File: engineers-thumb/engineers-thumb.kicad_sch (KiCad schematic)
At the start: 36 parts, among them J1 Barrel_Jack_Switch, J2 AudioJack3_Switch, Q1 BC556, Q2 J112, U1 ICL7660

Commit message: Intermittent eng thumb redux
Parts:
- added U? (x5): LM13700, symbol Amplifier_Operational:LM13700
- gave numbers to parts that had none: 13
- renumbered U1 to U2

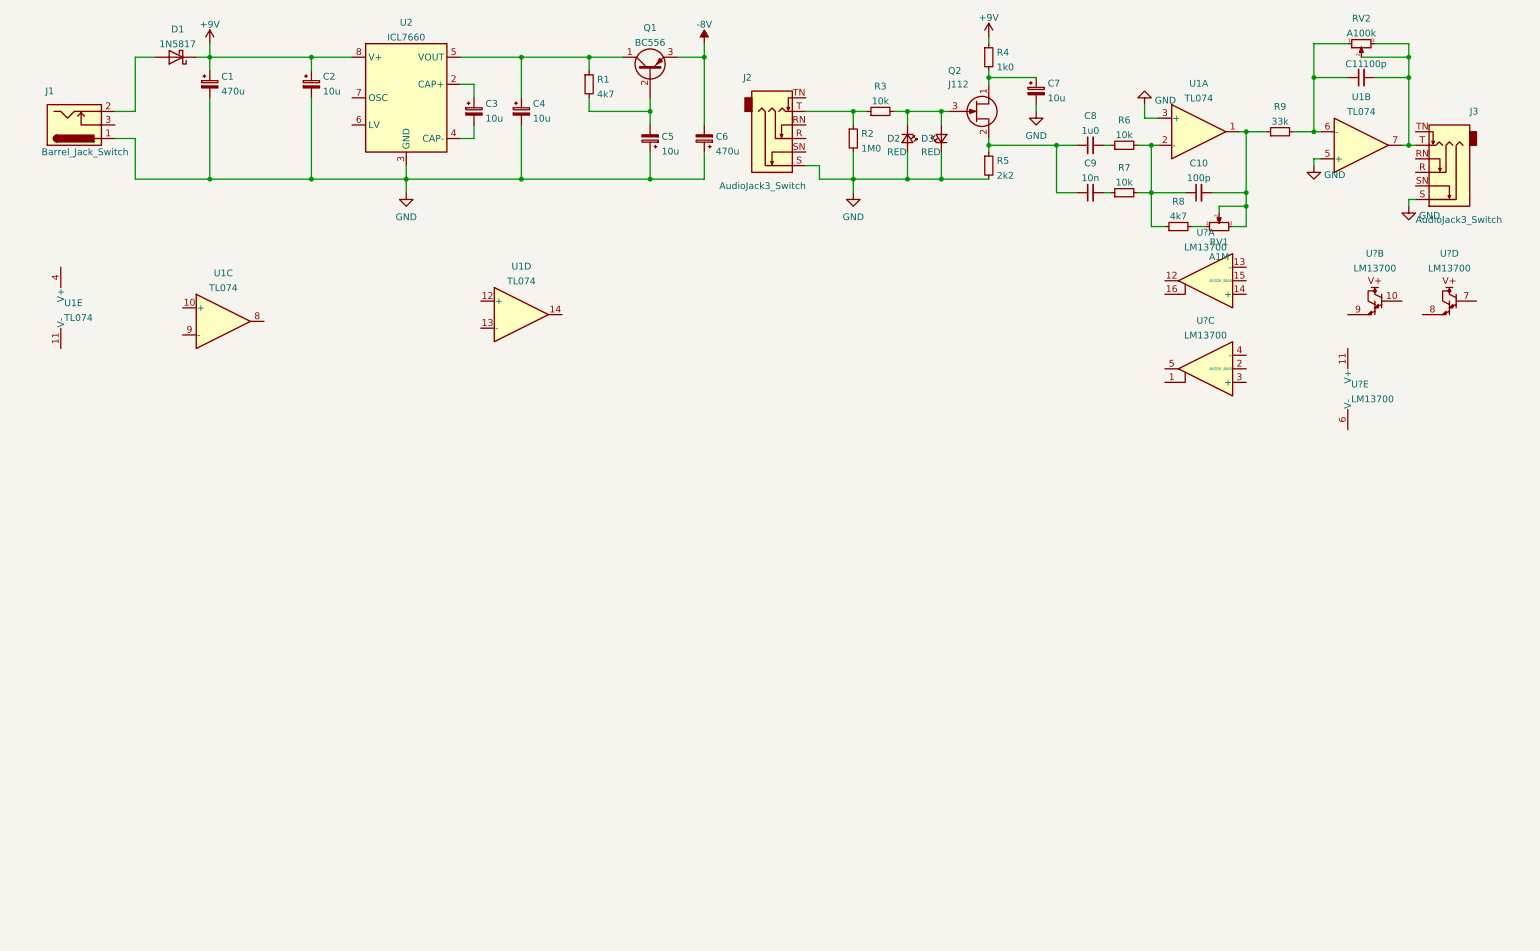
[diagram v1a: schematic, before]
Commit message: Engineers Thumb 1st. cancdidate
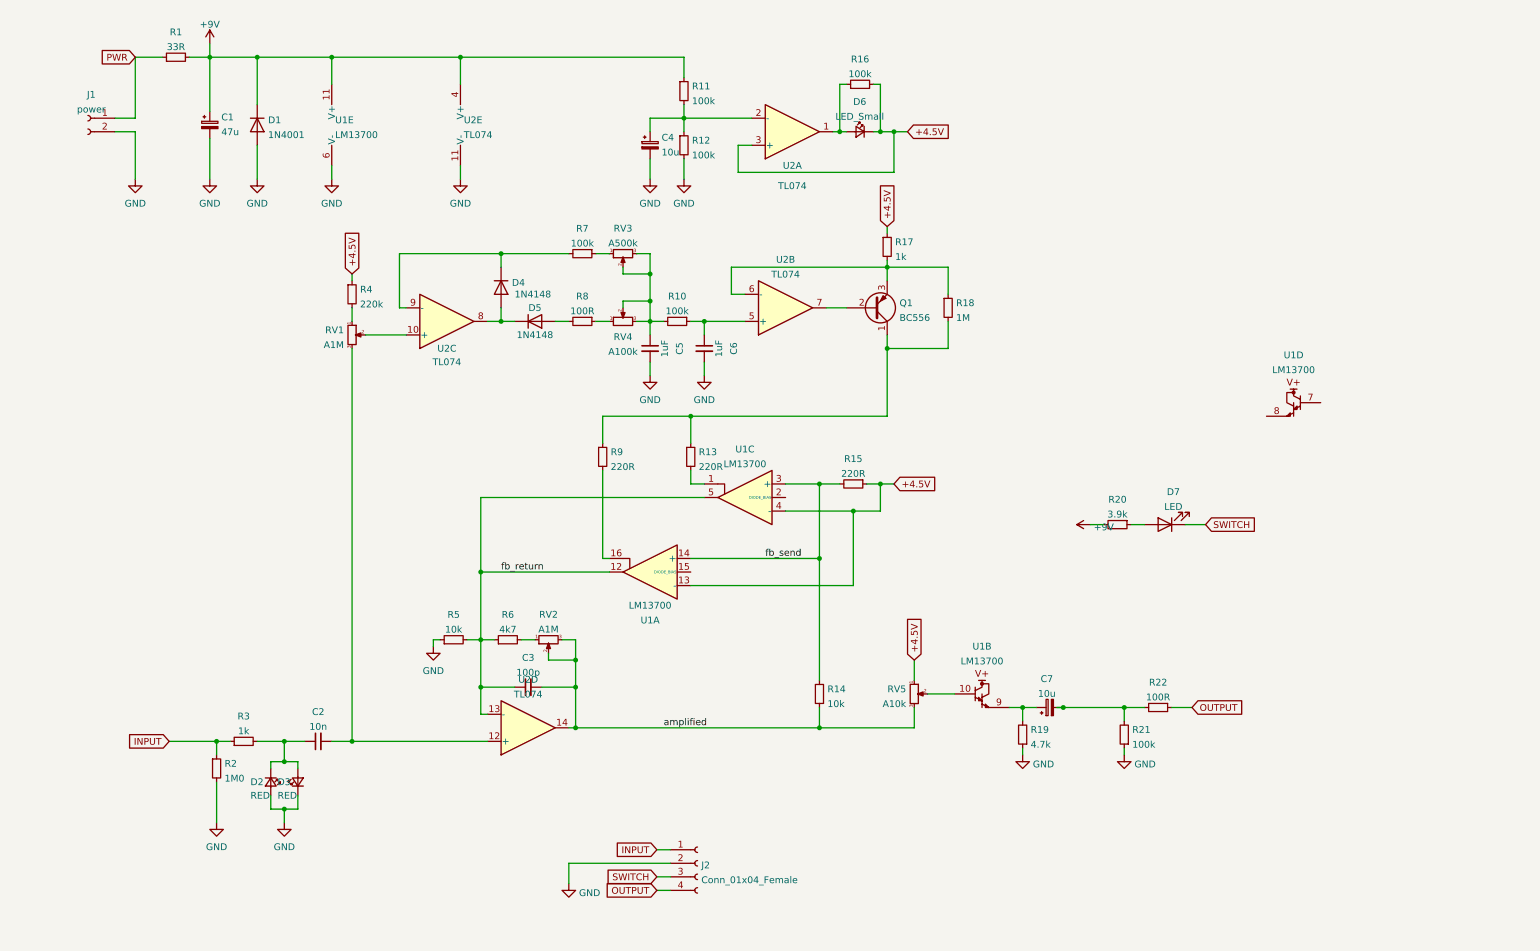
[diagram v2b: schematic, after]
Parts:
- removed C10, C11: 100p, Capacitor_THT:C_Disc_D5.0mm_W2.5mm_P2.50mm, symbol Device:C_Small
- removed C3, C4, C5: 10u, Capacitor_THT:CP_Radial_D5.0mm_P2.50mm, symbol Device:CP_Small
- removed C6: 470u, Capacitor_THT:CP_Radial_D10.0mm_P5.00mm, symbol Device:CP_Small
- removed C8: 1u0, Capacitor_THT:C_Rect_L7.0mm_W4.5mm_P5.00mm, symbol Device:C_Small
- removed D1: 1N5817, Diode_THT:D_DO-41_SOD81_P10.16mm_Horizontal, symbol Diode:1N5817
- removed J1: Barrel_Jack_Switch, Connector_BarrelJack:BarrelJack_Horizontal, symbol Connector:Barrel_Jack_Switch
- removed J2, J3: AudioJack3_Switch, PartsStash:Jack_6.35mm_Rean_NYS215_Horizontal, symbol Connector:AudioJack3_Switch
- removed Q2: J112, Package_TO_SOT_THT:TO-92L_Inline_Wide, symbol Transistor_FET:MMBFJ112
- removed U2: ICL7660, Package_DIP:DIP-8_W7.62mm_LongPads, symbol Regulator_SwitchedCapacitor:ICL7660
- added C3: 100p, Capacitor_THT:C_Disc_D5.0mm_W2.5mm_P2.50mm, symbol Device:C_Small
- added C5, C6: 1uF, Capacitor_THT:C_Rect_L7.0mm_W2.5mm_P5.00mm, symbol Device:C_Small
- added D1: 1N4001, Diode_THT:D_DO-41_SOD81_P10.16mm_Horizontal, symbol Diode:1N4001
- added D4, D5: 1N4148, Diode_THT:D_DO-35_SOD27_P7.62mm_Horizontal, symbol Diode:1N4148
- added D6: LED_Small, LED_THT:LED_D3.0mm_Clear, symbol Device:LED_Small
- added D7: LED, LED_THT:LED_D3.0mm, symbol Device:LED
- added J1: power, Connector_Wire:SolderWire-0.1sqmm_1x02_P3.6mm_D0.4mm_OD1mm, symbol Connector:Conn_01x02_Female
- added J2: Conn_01x04_Female, Connector_Wire:SolderWire-0.1sqmm_1x04_P3.6mm_D0.4mm_OD1mm, symbol Connector:Conn_01x04_Female
- added R10, R11, R12, R16, R21: 100k, PartsStash:R_Axial_DIN0207_L6.3mm_D2.5mm_P7.62mm_Horizontal, symbol Device:R_Small
- added R13, R15, R9: 220R, PartsStash:R_Axial_DIN0207_L6.3mm_D2.5mm_P7.62mm_Horizontal, symbol Device:R_Small
- added R14: 10k, PartsStash:R_Axial_DIN0207_L6.3mm_D2.5mm_P7.62mm_Horizontal, symbol Device:R_Small
- added R17: 1k, PartsStash:R_Axial_DIN0207_L6.3mm_D2.5mm_P7.62mm_Horizontal, symbol Device:R_Small
- added R18: 1M, PartsStash:R_Axial_DIN0207_L6.3mm_D2.5mm_P7.62mm_Horizontal, symbol Device:R_Small
- added R20: 3.9k, PartsStash:R_Axial_DIN0207_L6.3mm_D2.5mm_P7.62mm_Horizontal, symbol Device:R_Small
- added R22: 100R, PartsStash:R_Axial_DIN0207_L6.3mm_D2.5mm_P7.62mm_Horizontal, symbol Device:R_Small
- added RV2: A1M, Connector_PinHeader_2.54mm:PinHeader_1x03_P2.54mm_Vertical, symbol Device:R_POT_Small
- added RV3: A500k, Connector_PinHeader_2.54mm:PinHeader_1x03_P2.54mm_Vertical, symbol Device:R_POT_Small
- added RV4: A100k, Connector_PinHeader_2.54mm:PinHeader_1x03_P2.54mm_Vertical, symbol Device:R_POT_Small
- C1: value 470u -> 47u; footprint Capacitor_THT:CP_Radial_D10.0mm_P5.00mm -> Capacitor_THT:CP_Radial_D8.0mm_P3.50mm
- Q1: footprint Package_TO_SOT_THT:TO-92_Inline -> Package_TO_SOT_THT:TO-92_Inline_Wide
- R1: value 4k7 -> 33R
- R19: renamed from R9; value 33k -> 4.7k
- R3: value 10k -> 1k
- R4: value 1k0 -> 220k
- R5: value 2k2 -> 10k
- R6: value 10k -> 4k7
- R7: value 10k -> 100k
- R8: value 4k7 -> 100R
- RV5: renamed from RV2; value A100k -> A10k; footprint Connector_PinHeader_2.54mm:PinHeader_1x03_P2.54mm_Vertical -> Connector_Wire:SolderWire-0.1sqmm_1x03_P3.6mm_D0.4mm_OD1mm
- U1: renamed from U?; footprint (none) -> Package_DIP:DIP-16_W7.62mm_LongPads
- U2: renamed from U1; footprint (none) -> Package_DIP:DIP-14_W7.62mm_Socket_LongPads
- renumbered C9 to C2, C2 to C4
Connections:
- net +9V: now also R1.2, U1.11 (V+), U2.4 (V+), D1.1 (K), R11.1, R20.2; no longer C4.1, R4.1
- net GND: now also R19.1, R5.1, U1.6 (V-), U2.11 (V-), C5.2, C6.2, D1.2 (A), J1.2 (Pin_2), J2.2 (Pin_2), R12.2, R21.1; no longer C7.2, R5.2, U2.3 (+), U2.5 (+)
- net at C2.1: now also D2.1 (K), D3.2 (A), R3.2; no longer R5.1
- net fb_return: now reaches R6.1
- net fb_return: now also R5.2, U1.12, U1.5, U2.13 (-), C3.1
- net at Q1.2 (B): now also U2.7; no longer R1.2
- net at Q1.1 (C): now also R13.1, R18.2, R9.1; no longer R1.1
- net at R8.2: now also D5.2 (A); no longer RV1.1
- net +4.5V: now reaches U1.13 (-)
- net +4.5V: now also R4.1, RV5.1, U1.4 (-), U2.3 (+), D6.1 (K), R15.1, R16.2, R17.1
- net fb_send: now reaches U1.14 (+)
- net fb_send: now also U1.3 (+), R14.2, R15.2
- net at U1.16: now also R9.2
- net at C7.1: now also R19.2, U1.9; no longer R4.2
- net at U1.10: now also RV5.2
- net at U2.12 (+): now also C2.2, RV1.3
- net amplified: now reaches U2.14
- net amplified: now also RV5.3, C3.2, R14.1, RV2.2, RV2.3
- net at R7.1: now also RV3.1; no longer C2.2
- net INPUT: now reaches R2.1, R3.1
- net INPUT: now also J2.1 (Pin_1)
- net at U1.1: now also R13.2
- net at U2.10 (+): now also RV1.2
- net at U2.8: now also D4.2 (A), D5.1 (K)
- net at U2.9 (-): now also R7.2, D4.1 (K)
- net -8V: no longer names the net of Q1.3 (E)
- net -8V: now also U2.6 (-), R17.2, R18.1
- new net: C6.1, R10.1, U2.5 (+)
- new net: C5.1, R10.2, RV3.2, RV3.3, RV4.2, RV4.3
- new net: R8.1, RV4.1
- new net: C4.1, R11.2, R12.1, U2.2 (-)
- new net: D6.2 (A), R16.1, U2.1
- new net: C7.2, R21.2, R22.2
- new net: R6.2, RV2.1
- new net: D7.2 (A), R20.1
- new net: R4.2, RV1.1
- new net OUTPUT: J2.4 (Pin_4), R22.1
- new net PWR: J1.1 (Pin_1), R1.1
- new net SWITCH: D7.1 (K), J2.3 (Pin_3)
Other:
- moved on the sheet: C1, C2, C4, D2, D3, R19, R2, R3, R4, RV5, U1A, U1B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

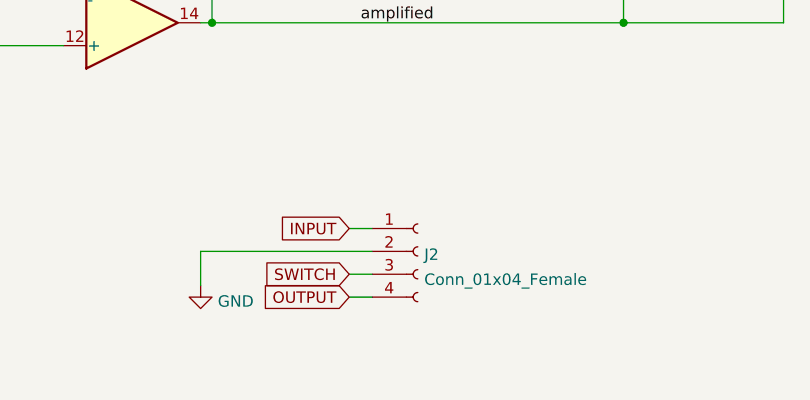
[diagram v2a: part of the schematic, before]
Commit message: Resized vias.
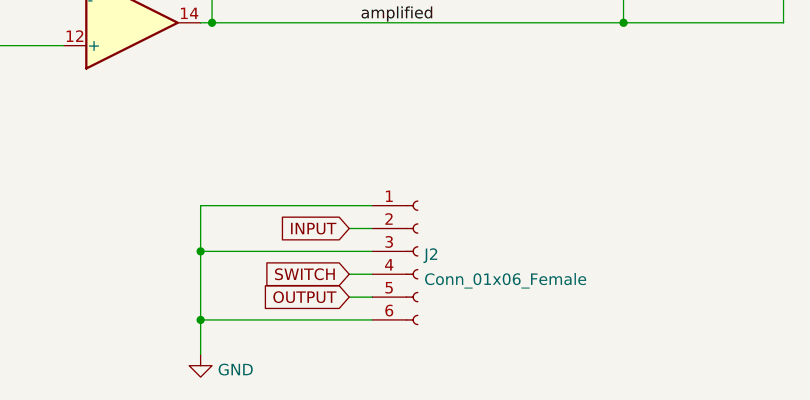
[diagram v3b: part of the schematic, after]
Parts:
- removed J2: Conn_01x04_Female, Connector_Wire:SolderWire-0.1sqmm_1x04_P3.6mm_D0.4mm_OD1mm, symbol Connector:Conn_01x04_Female
- added J2: Conn_01x06_Female, Connector_Wire:SolderWire-0.1sqmm_1x06_P3.6mm_D0.4mm_OD1mm, symbol Connector:Conn_01x06_Female
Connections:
- net GND: now also J2.1 (Pin_1), J2.3 (Pin_3), J2.6 (Pin_6)
- net INPUT: now also J2.2 (Pin_2)
- net OUTPUT: now also J2.5 (Pin_5)
- net SWITCH: now also J2.4 (Pin_4)
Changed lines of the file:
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@@
   (junction (at 139.7 69.85) (diameter 0) (color 0 0 0 0)
   )
+  (junction (at 114.3 171.45) (diameter 0) (color 0 0 0 0)
+  )
   (junction (at 173.99 74.93) (diameter 0) (color 0 0 0 0)
   )
@@
   (junction (at 218.44 142.24) (diameter 0) (color 0 0 0 0)
   )
+  (junction (at 114.3 179.07) (diameter 0) (color 0 0 0 0)
+  )
   (junction (at 115.57 133.35) (diameter 0) (color 0 0 0 0)
   )
@@
     (stroke (width 0) (type default) (color 0 0 0 0))
   )
+  (wire (pts (xy 114.3 166.37) (xy 114.3 171.45))
+    (stroke (width 0) (type default) (color 0 0 0 0))
+  )
   (wire (pts (xy 129.54 77.47) (xy 129.54 80.01))
     (stroke (width 0) (type default) (color 0 0 0 0))
@@
     (stroke (width 0) (type default) (color 0 0 0 0))
   )
+  (wire (pts (xy 114.3 179.07) (xy 114.3 182.88))
+    (stroke (width 0) (type default) (color 0 0 0 0))
+  )
   (wire (pts (xy 185.42 74.93) (xy 173.99 74.93))
     (stroke (width 0) (type default) (color 0 0 0 0))
@@
     (stroke (width 0) (type default) (color 0 0 0 0))
   )
+  (wire (pts (xy 114.3 179.07) (xy 133.35 179.07))
+    (stroke (width 0) (type default) (color 0 0 0 0))
+  )
+  (wire (pts (xy 133.35 166.37) (xy 114.3 166.37))
+    (stroke (width 0) (type default) (color 0 0 0 0))
+  )
   (wire (pts (xy 46.99 35.56) (xy 46.99 43.18))
     (stroke (width 0) (type default) (color 0 0 0 0))
@@
     (stroke (width 0) (type default) (color 0 0 0 0))
   )
-  (wire (pts (xy 114.3 171.45) (xy 114.3 175.26))
+  (wire (pts (xy 114.3 171.45) (xy 114.3 179.07))
     (stroke (width 0) (type default) (color 0 0 0 0))
   )
@@
   (symbol (lib_id "power:GND") (at 218.44 151.13 0) (unit 1)
     (in_bom yes) (on_board yes) (fields_autoplaced)
-    (property "Reference" "#PWR016" (id 0) (at 218.44 157.48 0)
+    (property "Reference" "#PWR017" (id 0) (at 218.44 157.48 0)
       (effects (font (size 1.27 1.27)) hide)
     )
@@
     (pin "9")
   )
-  (symbol (lib_id "Connector:Conn_01x04_Female") (at 138.43 171.45 0) (unit 1)
+  (symbol (lib_id "Connector:Conn_01x06_Female") (at 138.43 171.45 0) (unit 1)
     (in_bom yes) (on_board yes) (fields_autoplaced)
     (property "Reference" "J2" (id 0) (at 139.1412 171.8115 0)
       (effects (font (size 1.27 1.27)) (justify left))
     )
-    (property "Value" "Conn_01x04_Female" (id 1) (at 139.1412 174.5866 0)
-      (effects (font (size 1.27 1.27)) (justify left))
-    )
-    (property "Footprint" "Connector_Wire:SolderWire-0.1sqmm_1x04_P3.6mm_D0.4mm_OD1mm" (id 2) (at 138.43 171.45 0)
+    (property "Value" "Conn_01x06_Female" (id 1) (at 139.1412 174.5866 0)
+      (effects (font (size 1.27 1.27)) (justify left))
+    )
+    (property "Footprint" "Connector_Wire:SolderWire-0.1sqmm_1x06_P3.6mm_D0.4mm_OD1mm" (id 2) (at 138.43 171.45 0)
       (effects (font (size 1.27 1.27)) hide)
     )
@@
     (pin "3")
     (pin "4")
+    (pin "5")
+    (pin "6")
   )
   (symbol (lib_id "power:GND") (at 33.02 43.18 0) (unit 1)
@@
     (pin "3")
   )
-  (symbol (lib_id "power:GND") (at 114.3 175.26 0) (unit 1)
-    (in_bom yes) (on_board yes) (fields_autoplaced)
-    (property "Reference" "#PWR010" (id 0) (at 114.3 181.61 0)
-      (effects (font (size 1.27 1.27)) hide)
-    )
-    (property "Value" "GND" (id 1) (at 116.205 177.009 0)
-      (effects (font (size 1.27 1.27)) (justify left))
-    )
-    (property "Footprint" "" (id 2) (at 114.3 175.26 0)
-      (effects (font (size 1.27 1.27)) hide)
-    )
-    (property "Datasheet" "" (id 3) (at 114.3 175.26 0)
+  (symbol (lib_id "power:GND") (at 114.3 182.88 0) (unit 1)
+    (in_bom yes) (on_board yes) (fields_autoplaced)
+    (property "Reference" "#PWR010" (id 0) (at 114.3 189.23 0)
+      (effects (font (size 1.27 1.27)) hide)
+    )
+    (property "Value" "GND" (id 1) (at 116.205 184.629 0)
+      (effects (font (size 1.27 1.27)) (justify left))
+    )
+    (property "Footprint" "" (id 2) (at 114.3 182.88 0)
+      (effects (font (size 1.27 1.27)) hide)
+    )
+    (property "Datasheet" "" (id 3) (at 114.3 182.88 0)
       (effects (font (size 1.27 1.27)) hide)
     )
@@
   (symbol (lib_id "power:+9V") (at 212.09 107.95 90) (unit 1)
     (in_bom yes) (on_board yes) (fields_autoplaced)
-    (property "Reference" "#PWR0101" (id 0) (at 215.9 107.95 0)
+    (property "Reference" "#PWR016" (id 0) (at 215.9 107.95 0)
       (effects (font (size 1.27 1.27)) hide)
     )
@@
       (reference "#PWR015") (unit 1) (value "GND") (footprint "")
     )
+    (path "/bc08cc2e-1f07-4b04-a75d-496c3da1506c"
+      (reference "#PWR016") (unit 1) (value "+9V") (footprint "")
+    )
     (path "/17fb0478-2570-4dcd-a205-fc3721381945"
-      (reference "#PWR016") (unit 1) (value "GND") (footprint "")
-    )
-    (path "/bc08cc2e-1f07-4b04-a75d-496c3da1506c"
-      (reference "#PWR0101") (unit 1) (value "+9V") (footprint "")
+      (reference "#PWR017") (unit 1) (value "GND") (footprint "")
     )
     (path "/53bec0f2-2313-45ce-b2e6-76b7ab8701ed"
@@
       (reference "J1") (unit 1) (value "power") (footprint "Connector_Wire:SolderWire-0.1sqmm_1x02_P3.6mm_D0.4mm_OD1mm")
     )
-    (path "/5df6e7f5-fc69-4fee-a1ac-5648420950d4"
-      (reference "J2") (unit 1) (value "Conn_01x04_Female") (footprint "Connector_Wire:SolderWire-0.1sqmm_1x04_P3.6mm_D0.4mm_OD1mm")
+    (path "/5f88e7e8-608b-4cd5-88a1-58458c23b952"
+      (reference "J2") (unit 1) (value "Conn_01x06_Female") (footprint "Connector_Wire:SolderWire-0.1sqmm_1x06_P3.6mm_D0.4mm_OD1mm")
     )
     (path "/e34929be-df89-4480-911d-e2698e2f2477"
